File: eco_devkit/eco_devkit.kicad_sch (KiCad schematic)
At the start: 0 parts

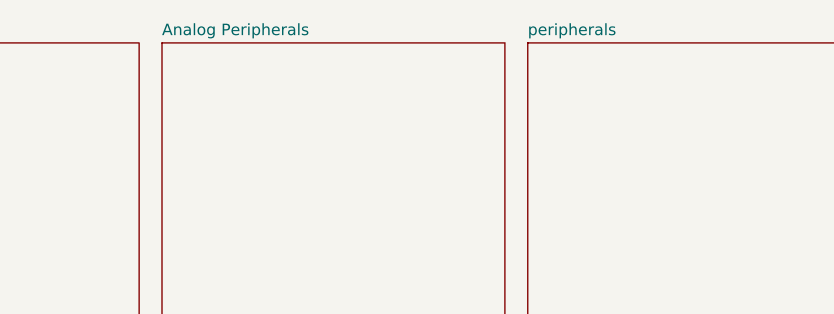
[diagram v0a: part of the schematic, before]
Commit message: Add bluetooth.
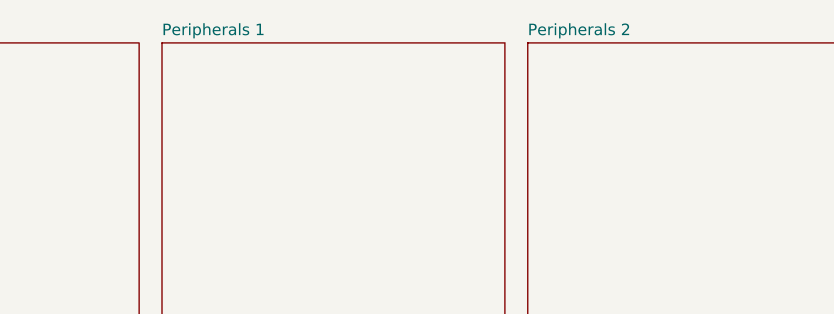
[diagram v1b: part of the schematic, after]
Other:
- sheet Analog Peripherals renamed Peripherals 1
- sheet peripherals renamed Peripherals 2
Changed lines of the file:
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@@
 			(color 0 0 0 0.0000)
 		)
-		(property "Sheetname" "peripherals"
+		(property "Sheetname" "Peripherals 2"
 			(at 232.41 75.4884 0)
 			(effects
@@
 			(color 0 0 0 0.0000)
 		)
-		(property "Sheetname" "Analog Peripherals"
+		(property "Sheetname" "Peripherals 1"
 			(at 191.77 75.4884 0)
 			(effects

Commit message: First interation.
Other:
- removed sheet Power Supply
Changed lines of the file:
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@@
 	)
 	(sheet
-		(at 29.21 76.2)
-		(size 38.1 38.1)
-		(exclude_from_sim no)
-		(in_bom yes)
-		(on_board yes)
-		(dnp no)
-		(fields_autoplaced yes)
-		(stroke
-			(width 0.1524)
-			(type solid)
-		)
-		(fill
-			(color 0 0 0 0.0000)
-		)
-		(property "Sheetname" "Power Supply"
-			(at 29.21 75.4884 0)
-			(effects
-				(font
-					(size 1.27 1.27)
-				)
-				(justify left bottom)
-			)
-		)
-		(property "Sheetfile" "power_supply.kicad_sch"
-			(at 29.21 114.8846 0)
-			(effects
-				(font
-					(size 1.27 1.27)
-				)
-				(justify left top)
-			)
-		)
-		(instances
-			(project "eco_devkit"
-				(path "/308cd3d6-c3d9-49fe-9127-06fda61df52b"
-					(page "2")
-				)
-			)
-		)
-	)
-	(sheet
-		(at 232.41 76.2)
+		(at 207.01 81.28)
 		(size 38.1 38.1)
 		(exclude_from_sim no)
@@
 		)
 		(property "Sheetname" "Peripherals 2"
-			(at 232.41 75.4884 0)
+			(at 207.01 80.5684 0)
 			(effects
 				(font
@@
 		)
 		(property "Sheetfile" "peripherals.kicad_sch"
-			(at 232.41 114.8846 0)
+			(at 207.01 119.9646 0)
 			(effects
 				(font
@@
 	)
 	(sheet
-		(at 191.77 76.2)
+		(at 166.37 81.28)
 		(size 38.1 38.1)
 		(exclude_from_sim no)
@@
 		)
 		(property "Sheetname" "Peripherals 1"
-			(at 191.77 75.4884 0)
+			(at 166.37 80.5684 0)
 			(effects
 				(font
@@
 		)
 		(property "Sheetfile" "analog_peripherals.kicad_sch"
-			(at 191.77 114.8846 0)
+			(at 166.37 119.9646 0)
 			(effects
 				(font
@@
 	)
 	(sheet
-		(at 110.49 76.2)
+		(at 85.09 81.28)
 		(size 38.1 38.1)
 		(exclude_from_sim no)
@@
 		)
 		(property "Sheetname" "MCU"
-			(at 110.49 75.4884 0)
+			(at 85.09 80.5684 0)
 			(effects
 				(font
@@
 		)
 		(property "Sheetfile" "mcu.kicad_sch"
-			(at 110.49 114.8846 0)
+			(at 85.09 119.9646 0)
 			(effects
 				(font
@@
 	)
 	(sheet
-		(at 69.85 76.2)
+		(at 44.45 81.28)
 		(size 38.1 38.1)
 		(exclude_from_sim no)
@@
 		)
 		(property "Sheetname" "Debug Probe"
-			(at 69.85 75.4884 0)
+			(at 44.45 80.5684 0)
 			(effects
 				(font
@@
 		)
 		(property "Sheetfile" "debug_probe.kicad_sch"
-			(at 69.85 114.8846 0)
+			(at 44.45 119.9646 0)
 			(effects
 				(font
@@
 	)
 	(sheet
-		(at 151.13 76.2)
+		(at 125.73 81.28)
 		(size 38.1 38.1)
 		(exclude_from_sim no)
@@
 		)
 		(property "Sheetname" "Bluetooth Module"
-			(at 151.13 75.4884 0)
+			(at 125.73 80.5684 0)
 			(effects
 				(font
@@
 		)
 		(property "Sheetfile" "bluetooth_module.kicad_sch"
-			(at 151.13 114.8846 0)
+			(at 125.73 119.9646 0)
 			(effects
 				(font

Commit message: Cria arquivo de backup.
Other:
- added sheet save (save.kicad_sch)
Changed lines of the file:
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@@
+		)
+	)
+	(sheet
+		(at 88.9 139.7)
+		(size 49.53 35.56)
+		(exclude_from_sim no)
+		(in_bom yes)
+		(on_board yes)
+		(dnp no)
+		(fields_autoplaced yes)
+		(stroke
+			(width 0.1524)
+			(type solid)
+		)
+		(fill
+			(color 0 0 0 0.0000)
+		)
+		(property "Sheetname" "save"
+			(at 88.9 138.9884 0)
+			(effects
+				(font
+					(size 1.27 1.27)
+				)
+				(justify left bottom)
+			)
+		)
+		(property "Sheetfile" "save.kicad_sch"
+			(at 88.9 175.8446 0)
+			(effects
+				(font
+					(size 1.27 1.27)
+				)
+				(justify left top)
+			)
+		)
+		(instances
+			(project "eco_devkit"
+				(path "/308cd3d6-c3d9-49fe-9127-06fda61df52b"
+					(page "7")
+				)
+			)
 		)
 	)
